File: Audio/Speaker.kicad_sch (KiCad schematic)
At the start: 6 parts, among them U1 NAU8315YG

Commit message: Rough placement of Speakers on board
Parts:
- added C14: 4u7, Capacitor_SMD:C_0201_0603Metric, symbol Device:C
- added C15: 0u1, Capacitor_SMD:C_0201_0603Metric, symbol Device:C
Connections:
- net +3V3: now also C14.2, C15.1
- net GND: now also C14.1, C15.2
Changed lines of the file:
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@@
 (kicad_sch (version 20211123) (generator eeschema)
   (paper "A5")
+  (junction (at 90.17 40.64) (diameter 0) (color 0 0 0 0)
+  )
   (junction (at 128.27 66.04) (diameter 0) (color 0 0 0 0)
   )
@@
     (stroke (width 0) (type default) (color 0 0 0 0))
   )
+  (wire (pts (xy 90.17 40.64) (xy 90.17 46.99))
+    (stroke (width 0) (type default) (color 0 0 0 0))
+  )
   (wire (pts (xy 106.68 59.69) (xy 107.95 59.69))
     (stroke (width 0) (type default) (color 0 0 0 0))
@@
     (stroke (width 0) (type default) (color 0 0 0 0))
   )
-  (wire (pts (xy 90.17 45.72) (xy 90.17 46.99))
+  (wire (pts (xy 88.9 40.64) (xy 90.17 40.64))
+    (stroke (width 0) (type default) (color 0 0 0 0))
+  )
+  (wire (pts (xy 90.17 24.13) (xy 90.17 40.64))
     (stroke (width 0) (type default) (color 0 0 0 0))
   )
@@
     (stroke (width 0) (type default) (color 0 0 0 0))
   )
+  (wire (pts (xy 92.71 40.64) (xy 90.17 40.64))
+    (stroke (width 0) (type default) (color 0 0 0 0))
+  )
   (wire (pts (xy 74.93 52.07) (xy 73.66 52.07))
     (stroke (width 0) (type default) (color 0 0 0 0))
@@
     (effects (font (size 1.27 1.27)) (justify right))
   )
-  (symbol (lib_id "power:+3V3") (at 90.17 45.72 0) (unit 1)
-    (in_bom yes) (on_board yes) (fields_autoplaced)
-    (property "Reference" "#PWR0117" (id 0) (at 90.17 49.53 0)
-      (effects (font (size 1.27 1.27)) hide)
-    )
-    (property "Value" "+3V3" (id 1) (at 90.17 40.64 0))
-    (property "Footprint" "" (id 2) (at 90.17 45.72 0)
-      (effects (font (size 1.27 1.27)) hide)
-    )
-    (property "Datasheet" "" (id 3) (at 90.17 45.72 0)
+  (symbol (lib_id "power:+3V3") (at 90.17 24.13 0) (unit 1)
+    (in_bom yes) (on_board yes) (fields_autoplaced)
+    (property "Reference" "#PWR0117" (id 0) (at 90.17 27.94 0)
+      (effects (font (size 1.27 1.27)) hide)
+    )
+    (property "Value" "+3V3" (id 1) (at 90.17 19.05 0))
+    (property "Footprint" "" (id 2) (at 90.17 24.13 0)
+      (effects (font (size 1.27 1.27)) hide)
+    )
+    (property "Datasheet" "" (id 3) (at 90.17 24.13 0)
       (effects (font (size 1.27 1.27)) hide)
     )
@@
     (pin "1")
   )
+  (symbol (lib_id "Device:C") (at 85.09 40.64 90) (unit 1)
+    (in_bom yes) (on_board yes) (fields_autoplaced)
+    (property "Reference" "C14" (id 0) (at 85.09 33.02 90))
+    (property "Value" "4u7" (id 1) (at 85.09 35.56 90))
+    (property "Footprint" "Capacitor_SMD:C_0201_0603Metric" (id 2) (at 88.9 39.6748 0)
+      (effects (font (size 1.27 1.27)) hide)
+    )
+    (property "Datasheet" "~" (id 3) (at 85.09 40.64 0)
+      (effects (font (size 1.27 1.27)) hide)
+    )
+    (pin "1")
+    (pin "2")
+  )
+  (symbol (lib_id "power:GND") (at 100.33 40.64 90) (unit 1)
+    (in_bom yes) (on_board yes) (fields_autoplaced)
+    (property "Reference" "#PWR0135" (id 0) (at 106.68 40.64 0)
+      (effects (font (size 1.27 1.27)) hide)
+    )
+    (property "Value" "GND" (id 1) (at 104.14 40.6399 90)
+      (effects (font (size 1.27 1.27)) (justify right))
+    )
+    (property "Footprint" "" (id 2) (at 100.33 40.64 0)
+      (effects (font (size 1.27 1.27)) hide)
+    )
+    (property "Datasheet" "" (id 3) (at 100.33 40.64 0)
+      (effects (font (size 1.27 1.27)) hide)
+    )
+    (pin "1")
+  )
   (symbol (lib_id "power:GND") (at 128.27 43.18 180) (unit 1)
     (in_bom yes) (on_board yes) (fields_autoplaced)
@@
     )
     (pin "1")
+  )
+  (symbol (lib_id "Device:C") (at 96.52 40.64 90) (unit 1)
+    (in_bom yes) (on_board yes) (fields_autoplaced)
+    (property "Reference" "C15" (id 0) (at 96.52 33.02 90))
+    (property "Value" "0u1" (id 1) (at 96.52 35.56 90))
+    (property "Footprint" "Capacitor_SMD:C_0201_0603Metric" (id 2) (at 100.33 39.6748 0)
+      (effects (font (size 1.27 1.27)) hide)
+    )
+    (property "Datasheet" "~" (id 3) (at 96.52 40.64 0)
+      (effects (font (size 1.27 1.27)) hide)
+    )
+    (pin "1")
+    (pin "2")
   )
   (symbol (lib_name "Speaker_1") (lib_id "Device:Speaker") (at 137.16 58.42 0) (unit 1)
@@
     (pin "9")
   )
+  (symbol (lib_id "power:GND") (at 81.28 40.64 270) (unit 1)
+    (in_bom yes) (on_board yes) (fields_autoplaced)
+    (property "Reference" "#PWR0136" (id 0) (at 74.93 40.64 0)
+      (effects (font (size 1.27 1.27)) hide)
+    )
+    (property "Value" "GND" (id 1) (at 77.47 40.6399 90)
+      (effects (font (size 1.27 1.27)) (justify right))
+    )
+    (property "Footprint" "" (id 2) (at 81.28 40.64 0)
+      (effects (font (size 1.27 1.27)) hide)
+    )
+    (property "Datasheet" "" (id 3) (at 81.28 40.64 0)
+      (effects (font (size 1.27 1.27)) hide)
+    )
+    (pin "1")
+  )
   (symbol (lib_id "Device:C") (at 128.27 46.99 0) (unit 1)

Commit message: Added Switches, Buttons, LEDs, 7Seg, LCD
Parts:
- renumbered C14 to C12, C15 to C13
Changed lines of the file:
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@@
   (symbol (lib_id "Device:C") (at 85.09 40.64 90) (unit 1)
     (in_bom yes) (on_board yes) (fields_autoplaced)
-    (property "Reference" "C14" (id 0) (at 85.09 33.02 90))
+    (property "Reference" "C12" (id 0) (at 85.09 33.02 90))
     (property "Value" "4u7" (id 1) (at 85.09 35.56 90))
     (property "Footprint" "Capacitor_SMD:C_0201_0603Metric" (id 2) (at 88.9 39.6748 0)
@@
   (symbol (lib_id "power:GND") (at 100.33 40.64 90) (unit 1)
     (in_bom yes) (on_board yes) (fields_autoplaced)
-    (property "Reference" "#PWR0135" (id 0) (at 106.68 40.64 0)
+    (property "Reference" "#PWR0133" (id 0) (at 106.68 40.64 0)
       (effects (font (size 1.27 1.27)) hide)
     )
@@
   (symbol (lib_id "Device:C") (at 96.52 40.64 90) (unit 1)
     (in_bom yes) (on_board yes) (fields_autoplaced)
-    (property "Reference" "C15" (id 0) (at 96.52 33.02 90))
+    (property "Reference" "C13" (id 0) (at 96.52 33.02 90))
     (property "Value" "0u1" (id 1) (at 96.52 35.56 90))
     (property "Footprint" "Capacitor_SMD:C_0201_0603Metric" (id 2) (at 100.33 39.6748 0)
@@
   (symbol (lib_id "power:GND") (at 81.28 40.64 270) (unit 1)
     (in_bom yes) (on_board yes) (fields_autoplaced)
-    (property "Reference" "#PWR0136" (id 0) (at 74.93 40.64 0)
+    (property "Reference" "#PWR0134" (id 0) (at 74.93 40.64 0)
       (effects (font (size 1.27 1.27)) hide)
     )

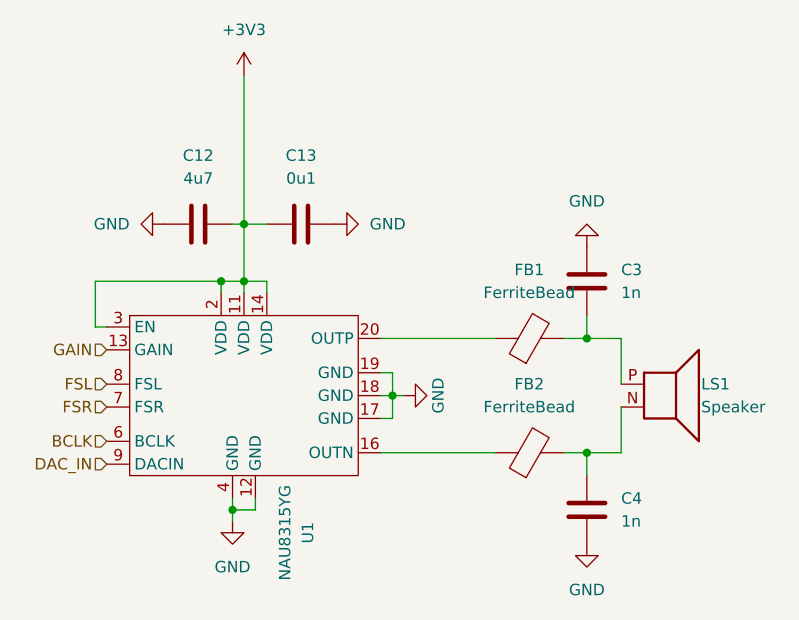
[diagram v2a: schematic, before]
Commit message: First week after winter break. Changed Power circuit design to use different DC to DC converter Setting correct footprints for the components like resistors and capacitors.
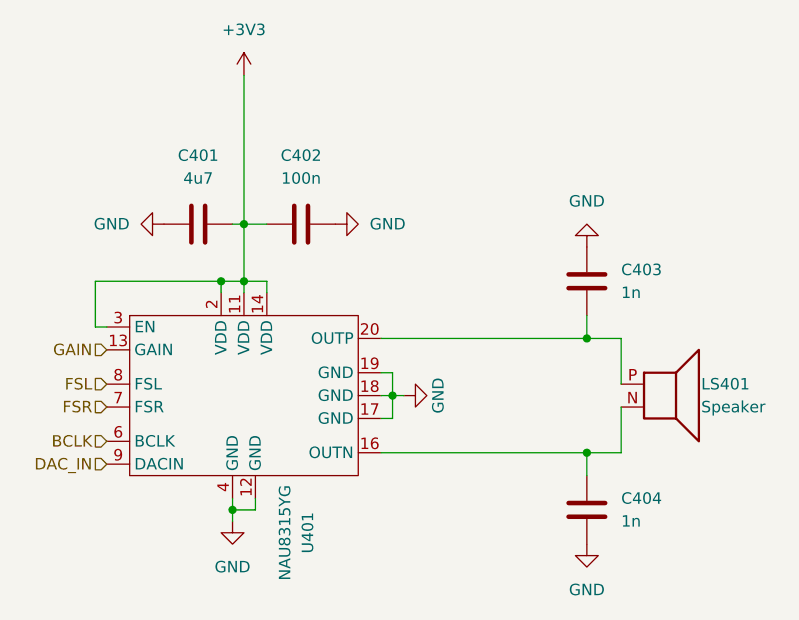
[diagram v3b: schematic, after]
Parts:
- removed FB1, FB2: FerriteBead, Inductor_SMD:L_0201_0603Metric, symbol Device:FerriteBead
- C401: renamed from C12; footprint Capacitor_SMD:C_0201_0603Metric -> Capacitor_SMD:C_0603_1608Metric; Manufacturer_Name (none) -> Samsung Electro-Mechanics; Manufacturer_Part_Number (none) -> CL10A475KO8NNNC
- C402: renamed from C13; value 0u1 -> 100n; footprint Capacitor_SMD:C_0201_0603Metric -> Capacitor_SMD:C_0805_2012Metric; Manufacturer_Name (none) -> Samsung Electro-Mechanics; Manufacturer_Part_Number (none) -> CL21B104KCFNNNE
- C403: renamed from C3; footprint Capacitor_SMD:C_0201_0603Metric -> Capacitor_SMD:C_0603_1608Metric; Manufacturer_Name (none) -> Samsung Electro-Mechanics; Manufacturer_Part_Number (none) -> CL10B102KB8NNNC
- C404: renamed from C4; footprint Capacitor_SMD:C_0201_0603Metric -> Capacitor_SMD:C_0603_1608Metric; Manufacturer_Name (none) -> Samsung Electro-Mechanics; Manufacturer_Part_Number (none) -> CL10B102KB8NNNC
- renumbered LS1 to LS401, U1 to U401
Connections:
- net at C404.1, LS401.N (2): now also U401.16 (OUTN)
- net at C403.2, LS401.P (1): now also U401.20 (OUTP); no longer U401.15 (NC)
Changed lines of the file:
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@@
-    (stroke (width 0) (type default) (color 0 0 0 0))
-  )
-  (wire (pts (xy 125.73 53.34) (xy 128.27 53.34))
     (stroke (width 0) (type default) (color 0 0 0 0))
   )
@@
     (stroke (width 0) (type default) (color 0 0 0 0))
   )
-  (wire (pts (xy 125.73 66.04) (xy 128.27 66.04))
+  (wire (pts (xy 105.41 66.04) (xy 128.27 66.04))
     (stroke (width 0) (type default) (color 0 0 0 0))
   )
@@
     (stroke (width 0) (type default) (color 0 0 0 0))
   )
-  (wire (pts (xy 118.11 53.34) (xy 105.41 53.34))
+  (wire (pts (xy 105.41 53.34) (xy 128.27 53.34))
     (stroke (width 0) (type default) (color 0 0 0 0))
   )
@@
     (stroke (width 0) (type default) (color 0 0 0 0))
   )
-  (wire (pts (xy 118.11 66.04) (xy 105.41 66.04))
-    (stroke (width 0) (type default) (color 0 0 0 0))
-  )
   (hierarchical_label "BCLK" (shape input) (at 74.93 64.77 180)
     (effects (font (size 1.27 1.27)) (justify right))
@@
   (symbol (lib_id "power:+3V3") (at 90.17 24.13 0) (unit 1)
     (in_bom yes) (on_board yes) (fields_autoplaced)
-    (property "Reference" "#PWR0117" (id 0) (at 90.17 27.94 0)
+    (property "Reference" "#PWR0403" (id 0) (at 90.17 27.94 0)
       (effects (font (size 1.27 1.27)) hide)
     )
@@
   (symbol (lib_id "power:GND") (at 128.27 76.2 0) (unit 1)
     (in_bom yes) (on_board yes) (fields_autoplaced)
-    (property "Reference" "#PWR0119" (id 0) (at 128.27 82.55 0)
+    (property "Reference" "#PWR0407" (id 0) (at 128.27 82.55 0)
       (effects (font (size 1.27 1.27)) hide)
     )
@@
   (symbol (lib_id "Device:C") (at 85.09 40.64 90) (unit 1)
     (in_bom yes) (on_board yes) (fields_autoplaced)
-    (property "Reference" "C12" (id 0) (at 85.09 33.02 90))
+    (property "Reference" "C401" (id 0) (at 85.09 33.02 90))
     (property "Value" "4u7" (id 1) (at 85.09 35.56 90))
-    (property "Footprint" "Capacitor_SMD:C_0201_0603Metric" (id 2) (at 88.9 39.6748 0)
+    (property "Footprint" "Capacitor_SMD:C_0603_1608Metric" (id 2) (at 88.9 39.6748 0)
       (effects (font (size 1.27 1.27)) hide)
     )
@@
       (effects (font (size 1.27 1.27)) hide)
     )
+    (property "Manufacturer_Name" "Samsung Electro-Mechanics" (id 4) (at 85.09 40.64 0)
+      (effects (font (size 1.27 1.27)) hide)
+    )
+    (property "Manufacturer_Part_Number" "CL10A475KO8NNNC" (id 5) (at 85.09 40.64 0)
+      (effects (font (size 1.27 1.27)) hide)
+    )
     (pin "1")
     (pin "2")
@@
   (symbol (lib_id "power:GND") (at 100.33 40.64 90) (unit 1)
     (in_bom yes) (on_board yes) (fields_autoplaced)
-    (property "Reference" "#PWR0133" (id 0) (at 106.68 40.64 0)
+    (property "Reference" "#PWR0404" (id 0) (at 106.68 40.64 0)
       (effects (font (size 1.27 1.27)) hide)
     )
@@
   (symbol (lib_id "power:GND") (at 128.27 43.18 180) (unit 1)
     (in_bom yes) (on_board yes) (fields_autoplaced)
-    (property "Reference" "#PWR0118" (id 0) (at 128.27 36.83 0)
+    (property "Reference" "#PWR0406" (id 0) (at 128.27 36.83 0)
       (effects (font (size 1.27 1.27)) hide)
     )
@@
   (symbol (lib_id "Device:C") (at 96.52 40.64 90) (unit 1)
     (in_bom yes) (on_board yes) (fields_autoplaced)
-    (property "Reference" "C13" (id 0) (at 96.52 33.02 90))
-    (property "Value" "0u1" (id 1) (at 96.52 35.56 90))
-    (property "Footprint" "Capacitor_SMD:C_0201_0603Metric" (id 2) (at 100.33 39.6748 0)
+    (property "Reference" "C402" (id 0) (at 96.52 33.02 90))
+    (property "Value" "100n" (id 1) (at 96.52 35.56 90))
+    (property "Footprint" "Capacitor_SMD:C_0805_2012Metric" (id 2) (at 100.33 39.6748 0)
       (effects (font (size 1.27 1.27)) hide)
     )
     (property "Datasheet" "~" (id 3) (at 96.52 40.64 0)
+      (effects (font (size 1.27 1.27)) hide)
+    )
+    (property "Manufacturer_Name" "Samsung Electro-Mechanics" (id 4) (at 96.52 40.64 0)
+      (effects (font (size 1.27 1.27)) hide)
+    )
+    (property "Manufacturer_Part_Number" "CL21B104KCFNNNE" (id 5) (at 96.52 40.64 0)
       (effects (font (size 1.27 1.27)) hide)
     )
@@
   (symbol (lib_name "Speaker_1") (lib_id "Device:Speaker") (at 137.16 58.42 0) (unit 1)
     (in_bom yes) (on_board yes)
-    (property "Reference" "LS1" (id 0) (at 140.97 58.42 0)
+    (property "Reference" "LS401" (id 0) (at 140.97 58.42 0)
       (effects (font (size 1.27 1.27)) (justify left))
     )
@@
     (pin "P")
   )
-  (symbol (lib_id "Device:FerriteBead") (at 121.92 53.34 90) (unit 1)
-    (in_bom yes) (on_board yes) (fields_autoplaced)
-    (property "Reference" "FB1" (id 0) (at 121.8692 45.72 90))
-    (property "Value" "FerriteBead" (id 1) (at 121.8692 48.26 90))
-    (property "Footprint" "Inductor_SMD:L_0201_0603Metric" (id 2) (at 121.92 55.118 90)
-      (effects (font (size 1.27 1.27)) hide)
-    )
-    (property "Datasheet" "~" (id 3) (at 121.92 53.34 0)
-      (effects (font (size 1.27 1.27)) hide)
-    )
-    (pin "1")
-    (pin "2")
-  )
   (symbol (lib_id "power:GND") (at 107.95 59.69 90) (unit 1)
     (in_bom yes) (on_board yes)
-    (property "Reference" "#PWR0120" (id 0) (at 114.3 59.69 0)
+    (property "Reference" "#PWR0405" (id 0) (at 114.3 59.69 0)
       (effects (font (size 1.27 1.27)) hide)
     )
@@
   (symbol (lib_id "Amplifier_Audio:NAU8315YG") (at 90.17 59.69 0) (unit 1)
     (in_bom yes) (on_board yes) (fields_autoplaced)
-    (property "Reference" "U1" (id 0) (at 97.2695 74.93 90))
+    (property "Reference" "U401" (id 0) (at 97.2695 74.93 90))
     (property "Value" "NAU8315YG" (id 1) (at 94.7295 74.93 90))
     (property "Footprint" "Custom:QFN50P400X400X80-21N" (id 2) (at 92.71 58.42 0)
@@
   (symbol (lib_id "power:GND") (at 81.28 40.64 270) (unit 1)
     (in_bom yes) (on_board yes) (fields_autoplaced)
-    (property "Reference" "#PWR0134" (id 0) (at 74.93 40.64 0)
+    (property "Reference" "#PWR0401" (id 0) (at 74.93 40.64 0)
       (effects (font (size 1.27 1.27)) hide)
     )
@@
   (symbol (lib_id "Device:C") (at 128.27 46.99 0) (unit 1)
     (in_bom yes) (on_board yes) (fields_autoplaced)
-    (property "Reference" "C3" (id 0) (at 132.08 45.7199 0)
+    (property "Reference" "C403" (id 0) (at 132.08 45.7199 0)
       (effects (font (size 1.27 1.27)) (justify left))
     )
@@
       (effects (font (size 1.27 1.27)) (justify left))
     )
-    (property "Footprint" "Capacitor_SMD:C_0201_0603Metric" (id 2) (at 129.2352 50.8 0)
+    (property "Footprint" "Capacitor_SMD:C_0603_1608Metric" (id 2) (at 129.2352 50.8 0)
       (effects (font (size 1.27 1.27)) hide)
     )
     (property "Datasheet" "~" (id 3) (at 128.27 46.99 0)
+      (effects (font (size 1.27 1.27)) hide)
+    )
+    (property "Manufacturer_Name" "Samsung Electro-Mechanics" (id 4) (at 128.27 46.99 0)
+      (effects (font (size 1.27 1.27)) hide)
+    )
+    (property "Manufacturer_Part_Number" "CL10B102KB8NNNC" (id 5) (at 128.27 46.99 0)
       (effects (font (size 1.27 1.27)) hide)
     )
@@
   (symbol (lib_id "Device:C") (at 128.27 72.39 0) (unit 1)
     (in_bom yes) (on_board yes)
-    (property "Reference" "C4" (id 0) (at 132.08 71.1199 0)
+    (property "Reference" "C404" (id 0) (at 132.08 71.1199 0)
       (effects (font (size 1.27 1.27)) (justify left))
     )
@@
       (effects (font (size 1.27 1.27)) (justify left))
     )
-    (property "Footprint" "Capacitor_SMD:C_0201_0603Metric" (id 2) (at 129.2352 76.2 0)
+    (property "Footprint" "Capacitor_SMD:C_0603_1608Metric" (id 2) (at 129.2352 76.2 0)
       (effects (font (size 1.27 1.27)) hide)
     )
@@
       (effects (font (size 1.27 1.27)) hide)
     )
+    (property "Manufacturer_Name" "Samsung Electro-Mechanics" (id 4) (at 128.27 72.39 0)
+      (effects (font (size 1.27 1.27)) hide)
+    )
+    (property "Manufacturer_Part_Number" "CL10B102KB8NNNC" (id 5) (at 128.27 72.39 0)
+      (effects (font (size 1.27 1.27)) hide)
+    )
     (pin "1")
     (pin "2")
@@
   (symbol (lib_id "power:GND") (at 88.9 73.66 0) (unit 1)
     (in_bom yes) (on_board yes) (fields_autoplaced)
-    (property "Reference" "#PWR0116" (id 0) (at 88.9 80.01 0)
+    (property "Reference" "#PWR0402" (id 0) (at 88.9 80.01 0)
       (effects (font (size 1.27 1.27)) hide)
     )
@@
     (pin "1")
   )
-  (symbol (lib_id "Device:FerriteBead") (at 121.92 66.04 90) (unit 1)
-    (in_bom yes) (on_board yes) (fields_autoplaced)
-    (property "Reference" "FB2" (id 0) (at 121.8692 58.42 90))
-    (property "Value" "FerriteBead" (id 1) (at 121.8692 60.96 90))
-    (property "Footprint" "Inductor_SMD:L_0201_0603Metric" (id 2) (at 121.92 67.818 90)
-      (effects (font (size 1.27 1.27)) hide)
-    )
-    (property "Datasheet" "~" (id 3) (at 121.92 66.04 0)
-      (effects (font (size 1.27 1.27)) hide)
-    )
-    (pin "1")
-    (pin "2")
-  )
 )

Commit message: Update BOM and POC files
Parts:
- LS401: Manufacturer_Name (none) -> PUI Audio, Inc.; Manufacturer_Part_Number (none) -> AS01508MS-SC11-WP-R
- U401: Manufacturer_Name (none) -> Nuvoton Technology Corporation; Manufacturer_Part_Number (none) -> NAU8315YG
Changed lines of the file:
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@@
+      (effects (font (size 1.27 1.27)) hide)
+    )
+    (property "Manufacturer_Name" "PUI Audio, Inc." (id 4) (at 137.16 58.42 0)
+      (effects (font (size 1.27 1.27)) hide)
+    )
+    (property "Manufacturer_Part_Number" "AS01508MS-SC11-WP-R" (id 5) (at 137.16 58.42 0)
       (effects (font (size 1.27 1.27)) hide)
     )
@@
       (effects (font (size 1.27 1.27)) hide)
     )
+    (property "Manufacturer_Name" "Nuvoton Technology Corporation" (id 4) (at 90.17 59.69 0)
+      (effects (font (size 1.27 1.27)) hide)
+    )
+    (property "Manufacturer_Part_Number" "NAU8315YG" (id 5) (at 90.17 59.69 0)
+      (effects (font (size 1.27 1.27)) hide)
+    )
